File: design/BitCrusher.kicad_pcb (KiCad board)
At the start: 2 copper layers, 181.5 x 86.2 mm, 138 parts, among them J1 BNC, J10 PJ-002BH, J2 BWSMA-KWE-Z001, J3 BWSMA-KE-Z001, J4 BWSMA-KE-Z001, J5 SHOU HAN TYPE-C 14P CC-2.6, J6 Conn_01x04_Pin, J7 Conn_01x04_Pin, J8 Conn_01x03_Pin, J9 Conn_01x03_Pin, Q1 SW4N60, Q2 2SA1213, Q3 GAN080-650EBE, T1 DA2033-AL, U1 STM32F303RETx, U2 USBLC6-2SC6, U3 FT230XQ, U4 TPS7A2050PDQN, U5 TPS7A2033PDQN, U6 LMR33630ADDA, U7 LMR33630ADDA, U8 TLP152TPL_E, U9 MAX22702EASA+

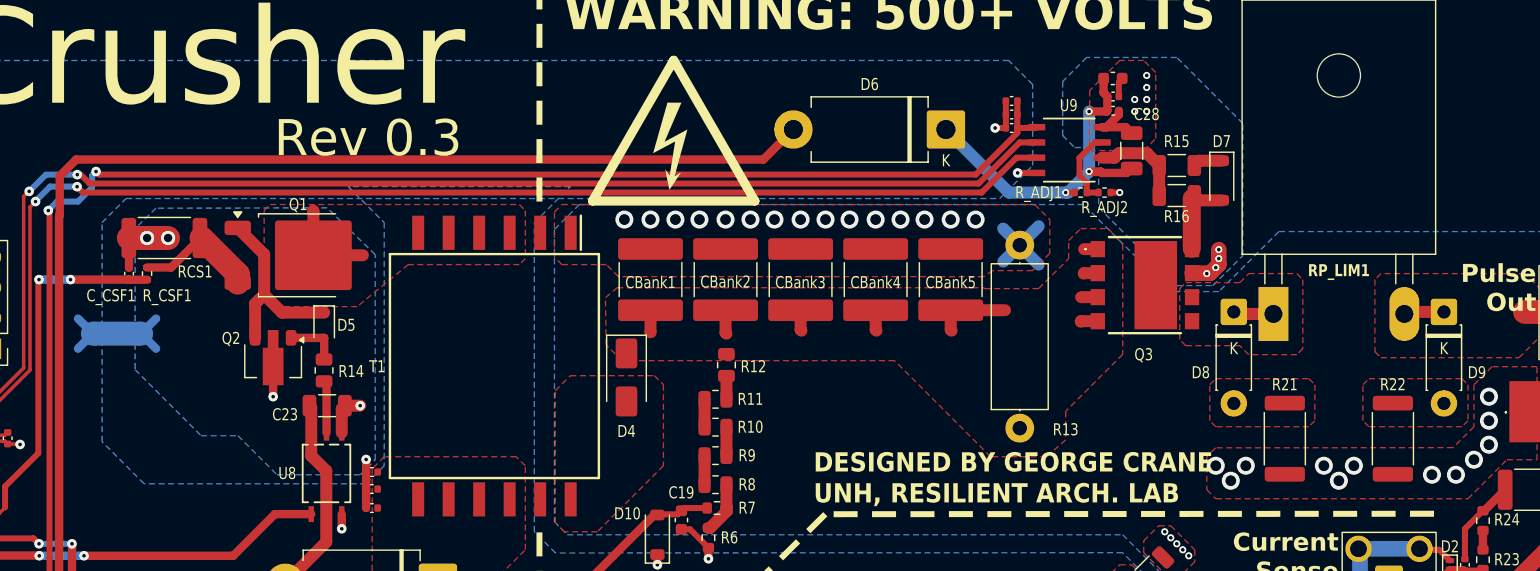
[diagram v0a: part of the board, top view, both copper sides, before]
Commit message: Replace HV bootstrap diode with properly spec'd fast recovery diode
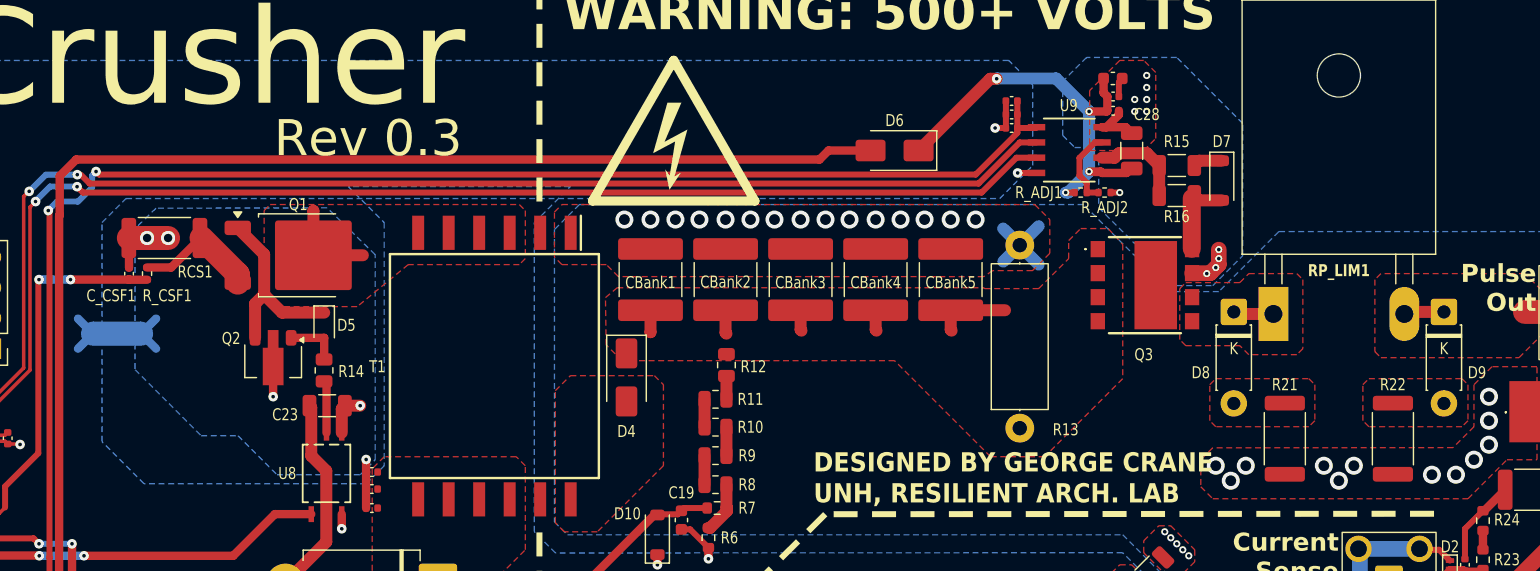
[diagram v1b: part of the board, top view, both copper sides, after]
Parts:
- D1, D2: value SP3031-01ETG -> SP3130-01ETG
- D11: value SMBJ20A -> SMBJ26A
- D6: value 1N5822 -> ES1M; footprint Diode_THT:D_DO-201AD_P12.70mm_Horizontal -> Diode_SMD:D_SMA
- moved D6 4.62 mm to (176.0, 71.2)
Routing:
- net +6V: track 142.3 -> 148.0 mm
- net /High Voltage Switching/VDD_DRV: track 28.7 -> 34.4 mm, vias 3 -> 4
- net HV+: track 19.1 -> 14.0 mm

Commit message: reshaping board
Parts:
- moved H1 3.00 mm to (66.5, 135.5)
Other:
- board outline removed

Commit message: Pour optimization
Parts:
- moved R25 1.94 mm to (231.8, 99.5)
- moved D7 0.25 mm to (203.0, 73.8)
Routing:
- net PulseCS-: track 46.6 -> 38.1 mm, vias 32 -> 37
- net HV+: track 14.0 -> 7.29 mm
- net Probe-: track 1.27 -> 5.10 mm
- net GND_DRV: track 11.0 -> 7.56 mm, vias 11 -> 10
- net /High Voltage Switching/HVSW+: track 3.72 -> 0.59 mm
- net Probe+: track 43.6 -> 40.4 mm
- net Net-(C34-Pad2): track 7.63 -> 9.15 mm
- net Net-(D7-A): track 7.01 -> 7.75 mm

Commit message: New outline
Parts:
- moved H3 20.8 mm to (241.5, 135.5)
- moved H2 8.50 mm to (241.5, 60.5)
- moved C32 7.50 mm to (231.0, 113.0)
- moved C33 7.50 mm to (231.0, 115.5)
- moved C34 7.50 mm to (231.0, 105.8)
- moved D1 7.50 mm to (229.8, 116.2)
- moved D2 7.50 mm to (229.8, 105.8)
- moved D8 7.50 mm to (211.8, 84.7)
- moved D9 7.50 mm to (229.2, 84.7)
- moved J2 7.50 mm to (241.1, 84.8)
- moved J3 7.50 mm to (224.7, 117.3)
- moved J4 7.50 mm to (224.7, 107.0)
- moved R17 7.50 mm to (232.5, 110.2)
- moved R18 7.50 mm to (232.5, 113.4)
- moved R19 7.50 mm to (232.5, 116.7)
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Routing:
- net Probe-: track 5.10 -> 0.00 mm
- net /High Voltage Switching/VDD_DRV: track 34.4 -> 30.2 mm
- net Probe+: track 40.4 -> 44.0 mm
- net GND: track 89.9 -> 92.2 mm
- net /High Voltage Switching/HVSW+: track 0.59 -> 0.00 mm
- added copper zone on B.Cu, net Probe+
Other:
- board outline added: 190 x 90 mm

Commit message: added missing 3D models
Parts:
- U8: value TLP152TPL_E -> e
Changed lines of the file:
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@@
 			)
 		)
-		(property "Value" "TLP152TPL_E"
+		(property "Value" "e"
 			(at 0 0 90)
 			(unlocked yes)
@@
 		)
 		(embedded_fonts no)
+		(model "${KIPRJMOD}/3d-models/TLP152_TPL,E.stp"
+			(offset
+				(xyz 0 0 0)
+			)
+			(scale
+				(xyz 1 1 1)
+			)
+			(rotate
+				(xyz 0 0 0)
+			)
+		)
 	)
 	(footprint "Capacitor_SMD:C_0402_1005Metric"
@@
 		)
 		(embedded_fonts no)
-		(model "WSHP2818R0200FEA.stp"
+		(model "${KIPRJMOD}/3d-models/WSHP2818R0200FEA.stp"
 			(offset
 				(xyz 0 -2.299999918 0.1500000037)
@@
 		)
 		(embedded_fonts no)
+		(model "${KIPRJMOD}/3d-models/21-0041-A_8L.step"
+			(offset
+				(xyz 0 0 0)
+			)
+			(scale
+				(xyz 1 1 1)
+			)
+			(rotate
+				(xyz 0 0 0)
+			)
+		)
 	)
 	(footprint "Capacitor_SMD:C_0402_1005Metric"

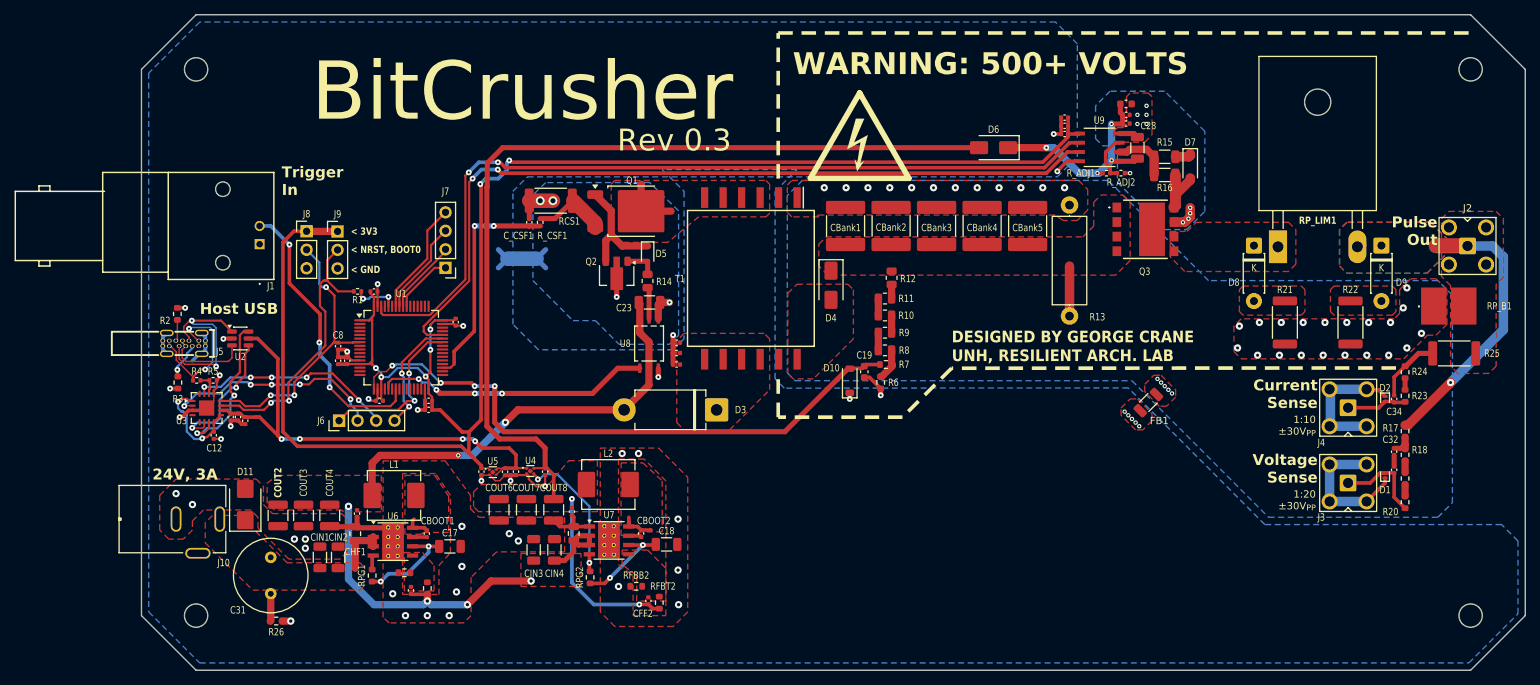
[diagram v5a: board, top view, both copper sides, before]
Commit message: top side ground plane
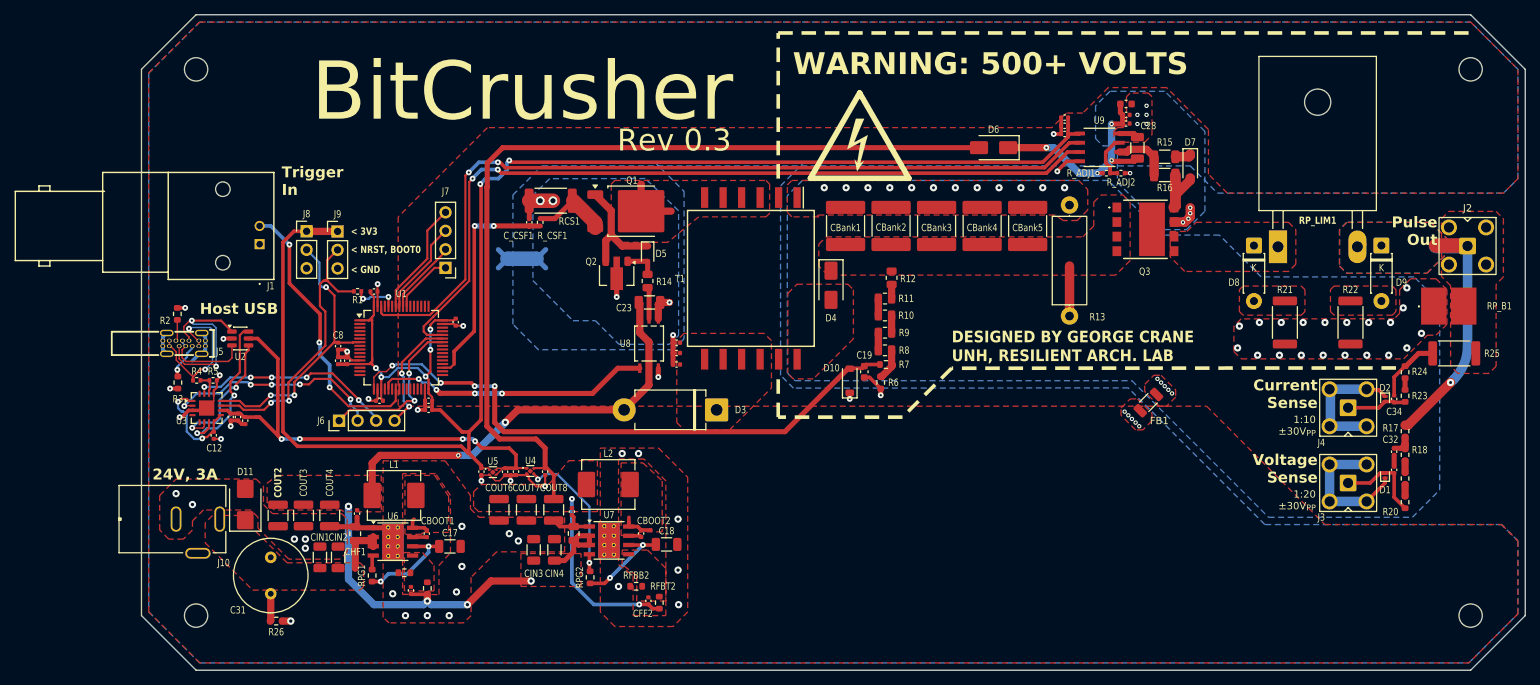
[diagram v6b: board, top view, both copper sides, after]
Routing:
- net Probe+: track 44.0 -> 37.6 mm
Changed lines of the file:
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@@
 			(net "Net-(D3-K)")
 			(pintype "passive")
+			(thermal_bridge_width 0.7)
+			(thermal_gap 0.4)
 		)
 		(pad "8" smd rect
@@
 			(net "Net-(D3-K)")
 			(pintype "passive")
+			(thermal_bridge_width 0.7)
+			(thermal_gap 0.4)
 		)
 		(pad "9" smd rect
@@
 			(net "Net-(D3-K)")
 			(pintype "passive")
+			(thermal_bridge_width 0.7)
+			(thermal_gap 0.4)
 		)
 		(pad "10" smd rect
@@
 			(net "Net-(D3-K)")
 			(pintype "passive")
+			(thermal_bridge_width 0.7)
+			(thermal_gap 0.4)
 		)
 		(pad "11" smd rect
@@
 	)
 	(segment
-		(start 246 86.25)
-		(end 244.5 84.75)
-		(width 1.3)
-		(layer "B.Cu")
-		(net "Probe+")
-	)
-	(segment
-		(start 238.75 103.5)
-		(end 246 96.25)
+		(start 239.183489 103.06651)
+		(end 238.75 103.5)
 		(width 1.3)
 		(layer "B.Cu")
@@
 	)
 	(segment
-		(start 246 96.25)
-		(end 246 86.25)
-		(width 1.3)
+		(start 241.075 84.75)
+		(end 236.75 84.75)
+		(width 2)
 		(layer "B.Cu")
 		(net "Probe+")
@@
 	(segment
 		(start 241.075 84.75)
-		(end 236.75 84.75)
-		(width 2)
+		(end 241.075 98.5)
+		(width 1.3)
 		(layer "B.Cu")
 		(net "Probe+")
 	)
-	(segment
-		(start 244.5 84.75)
-		(end 241.075 84.75)
+	(arc
+		(start 241.075 98.5)
+		(mid 240.583412 100.971378)
+		(end 239.183489 103.06651)
 		(width 1.3)
 		(layer "B.Cu")
@@
 		(layer "F.Cu")
 		(hatch edge 0.5)
+		(priority 1)
 		(connect_pads
 			(clearance 0.5)
@@
 		(layer "F.Cu")
 		(hatch edge 0.5)
-		(priority 9)
+		(priority 10)
 		(connect_pads
 			(clearance 0.5)
@@
 		(layer "F.Cu")
 		(hatch edge 0.5)
-		(priority 26)
+		(priority 25)
 		(connect_pads
 			(clearance 0.3)
@@
 		(layer "F.Cu")
 		(hatch edge 0.5)
-		(priority 25)
+		(priority 24)
 		(connect_pads
 			(clearance 0.5)
@@
 		(layer "F.Cu")
 		(hatch edge 0.5)
-		(priority 1)
+		(priority 2)
 		(connect_pads
 			(clearance 0.5)
@@
 		(layer "F.Cu")
 		(hatch edge 0.5)
-		(priority 2)
+		(priority 3)
 		(connect_pads
 			(clearance 0.5)
@@
 		(hatch edge 0.5)
 		(priority 28)
-		(connect_pads yes
-			(clearance 0.3)
+		(connect_pads
+			(clearance 0.2)
 		)
-		(min_thickness 0.25)
+		(min_thickness 0.2)
 		(fill yes
-			(thermal_gap 0.5)
+			(thermal_gap 0.1)
 			(thermal_bridge_width 0.5)
 			(island_removal_mode 0)
@@
 	)
 	(zone
+		(net "GND")
+		(layer "F.Cu")
+		(hatch edge 0.5)
+		(connect_pads
+			(clearance 0.5)
+		)
+		(min_thickness 0.25)
+		(fill yes
+			(thermal_gap 0.5)
+			(thermal_bridge_width 0.5)
+			(island_removal_mode 0)
+		)
+		(polygon
+			(pts
+				(xy 246 77.5) (xy 208.1 77.5) (xy 205.5 74.9) (xy 205.5 68.75) (xy 199.75 63) (xy 191.75 63) (xy 188.25 66.5)
+				(xy 186 66.5) (xy 184 68.5) (xy 106.5 68.5) (xy 94.25 80.75) (xy 94.25 106.75) (xy 205.25 106.75)
+				(xy 221.5 123) (xy 245.75 123) (xy 248 125.25) (xy 248 135.25) (xy 241.25 142) (xy 67 142) (xy 60 135)
+				(xy 60 61) (xy 67 54) (xy 241.5 54) (xy 248 60.5) (xy 248 75.5)
+			)
+		)
+	)
+	(zone
 		(net "Net-(U7-FB)")
 		(layer "F.Cu")
 		(hatch edge 0.5)
-		(priority 4)
+		(priority 5)
 		(connect_pads
 			(clearance 0.5)
@@
 		(layer "F.Cu")
 		(hatch edge 0.5)
-		(priority 11)
+		(priority 12)
 		(connect_pads
 			(clearance 0.5)
@@
 		(layer "F.Cu")
 		(hatch edge 0.5)
-		(priority 21)
+		(priority 20)
 		(connect_pads
 			(clearance 0.5)
@@
 		(layer "F.Cu")
 		(hatch edge 0.5)
-		(priority 10)
+		(priority 11)
 		(connect_pads
 			(clearance 0.5)
@@
 		(layer "F.Cu")
 		(hatch edge 0.5)
-		(priority 6)
+		(priority 7)
 		(connect_pads
 			(clearance 0.5)
@@
 		(layer "F.Cu")
 		(hatch edge 0.5)
-		(priority 22)
+		(priority 21)
 		(connect_pads
 			(clearance 0.5)
@@
 		(layer "F.Cu")
 		(hatch edge 0.5)
-		(priority 19)
+		(priority 18)
 		(connect_pads yes
 			(clearance 0.5)
@@
 		(layer "F.Cu")
 		(hatch edge 0.5)
-		(priority 12)
+		(priority 13)
 		(connect_pads
 			(clearance 0.5)
@@
 		(layer "F.Cu")
 		(hatch edge 0.5)
-		(priority 5)
+		(priority 6)
 		(connect_pads
 			(clearance 0.5)
@@
 		(layer "F.Cu")
 		(hatch edge 0.5)
-		(priority 13)
+		(priority 29)
 		(connect_pads
 			(clearance 0.5)
@@
 		(polygon
 			(pts
-				(xy 145.25 97.5) (xy 144.5 96.75) (xy 133.5 96.75) (xy 132.5 97.75) (xy 132.5 109) (xy 133.5 110)
-				(xy 139.75 110) (xy 145.25 104.5)
+				(xy 145.5 97.75) (xy 144.5 96.75) (xy 133.5 96.75) (xy 132.5 97.75) (xy 132.5 109) (xy 133.5 110)
+				(xy 139.75 110) (xy 145.5 104.25)
 			)
 		)
@@
 		(layer "F.Cu")
 		(hatch edge 0.5)
-		(priority 23)
+		(priority 22)
 		(connect_pads
 			(clearance 0.5)
@@
 		(layer "F.Cu")
 		(hatch edge 0.5)
-		(priority 7)
+		(priority 8)
 		(connect_pads
 			(clearance 0.5)
@@
 		(layer "F.Cu")
 		(hatch edge 0.5)
-		(priority 24)
+		(priority 23)
 		(connect_pads
 			(clearance 0.5)
@@
 		(layer "F.Cu")
 		(hatch edge 0.5)
-		(priority 8)
+		(priority 9)
 		(connect_pads
 			(clearance 0.2)
@@
 		(layer "F.Cu")
 		(hatch edge 0.5)
-		(priority 18)
+		(priority 17)
 		(connect_pads
 			(clearance 0.5)
@@
 		(layer "F.Cu")
 		(hatch edge 0.5)
-		(priority 3)
+		(priority 4)
 		(connect_pads
 			(clearance 0.5)
@@
 		(layers "F.Cu" "B.Cu")
 		(hatch edge 0.5)
-		(priority 20)
+		(priority 19)
 		(connect_pads yes
 			(clearance 0.5)
@@
 		(layer "B.Cu")
 		(hatch edge 0.5)
-		(priority 16)
+		(priority 15)
 		(connect_pads
 			(clearance 0.5)
@@
 		(polygon
 			(pts
-				(xy 121.317693 95) (xy 124.567911 98.25) (xy 131.5 98.25) (xy 132.75 97) (xy 132.75 79.92197) (xy 128.7475 76.026821)
-				(xy 114.5 76.051183) (xy 112.75 77.75) (xy 112.75 89.5) (xy 118.25 95)
+				(xy 121.317693 95) (xy 124.567911 98.25) (xy 131.5 98.25) (xy 132.75 97) (xy 132.75 79.92197) (xy 128.194835 75.488979)
+				(xy 115.055999 75.511446) (xy 112.75 77.75) (xy 112.75 89.5) (xy 118.25 95)
 			)
 		)
@@
 		(layer "B.Cu")
 		(hatch edge 0.5)
-		(priority 17)
+		(priority 16)
 		(connect_pads
 			(clearance 0.5)
@@
 		(polygon
 			(pts
-				(xy 147.675 102.175) (xy 148.75 103.25) (xy 195 103.25) (xy 213.75 122) (xy 237 122) (xy 239 120)
-				(xy 239 91.500153) (xy 237.000153 89.5) (xy 205.506588 89.5) (xy 191.742652 75.75) (xy 149.75 75.75)
-				(xy 147.675 77.825)
+				(xy 147.675 102.175) (xy 148.75 103.25) (xy 195 103.25) (xy 213.75 122) (xy 233.5 122) (xy 237.25 118.25)
+				(xy 237.25 92.500268) (xy 233.751086 89.000816) (xy 212.746928 88.996784) (xy 206.999868 83.25)
+				(xy 199.250253 83.25) (xy 191.742652 75.75) (xy 149.75 75.75) (xy 147.675 77.825)
 			)
 		)
@@
 		(layer "B.Cu")
 		(hatch edge 0.5)
-		(priority 15)
+		(priority 14)
 		(connect_pads
 			(clearance 0.5)
@@
 				(xy 66.998035 54.001967) (xy 59.9948 61.005202) (xy 59.9948 134.990093) (xy 66.99523 141.999923)
 				(xy 241.25 142.000004) (xy 248 135.25) (xy 248 125.25) (xy 245.75 123) (xy 213.250051 123) (xy 194.491314 104.239347)
-				(xy 147.268993 104.268546) (xy 146 103.001681) (xy 146 77.250002) (xy 149.000002 74.25) (xy 130.5 74.25)
-				(xy 133.5 77.25) (xy 133.5 97.5) (xy 132 99) (xy 113.5 99) (xy 110 95.5) (xy 110 77.24922) (xy 112.000871 75.249911)
-				(xy 184.749906 75.250094) (xy 187.5 72.5) (xy 187.5 57) (xy 184.498033 53.998033)
+				(xy 148.519901 104.267773) (xy 146.75 102.50084) (xy 146.75 76.500002) (xy 150.000002 73.25) (xy 129.5 73.25)
+				(xy 133.5 77.25) (xy 133.5 97.5) (xy 132 99) (xy 113.5 99) (xy 110 95.5) (xy 110 77.75) (xy 114 73.75)
+				(xy 203 73.75) (xy 206.75 77.5) (xy 246 77.5) (xy 248 75.5) (xy 248 60.5) (xy 241.499997 53.999997)
 			)
 		)

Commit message: GND plane via stitching
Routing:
- net Probe+: track 37.6 -> 33.3 mm
- net GND: track 92.2 -> 91.0 mm, vias 46 -> 123
- net GNDFLY: track 21.8 -> 22.5 mm, vias 5 -> 11
- net +22V: vias 6 -> 7
- added copper zone on F.Cu, net GNDFLY
- removed copper zone on B.Cu, net Probe+
